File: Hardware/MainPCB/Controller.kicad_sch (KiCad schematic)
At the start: 31 parts, among them J10 Conn_01x02_Male, J11 Conn_01x11_Male, SW1 SW_Push, SW2 SW_Push, SW3 SW_Push, SW4 SW_Push, U5 CP2102N-Axx-xQFN28, U6 ATmega4809-A, U7 LMH1980

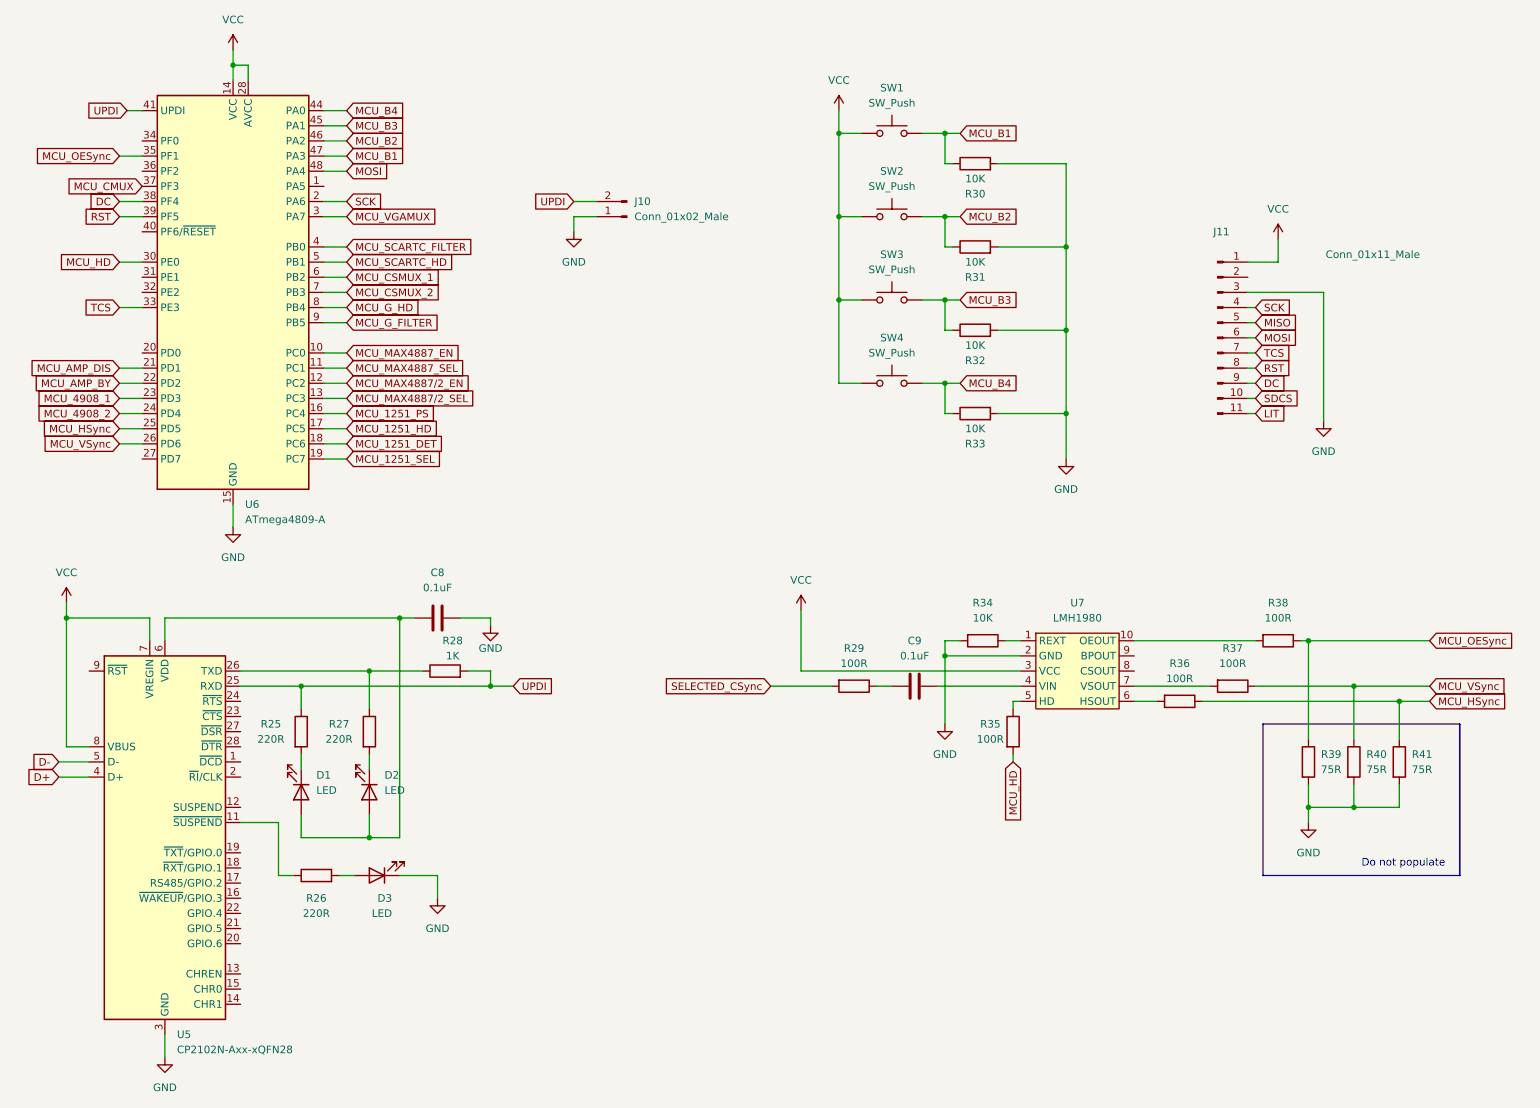
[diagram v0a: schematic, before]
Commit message: Fixed color bending issue; Added diagnostics
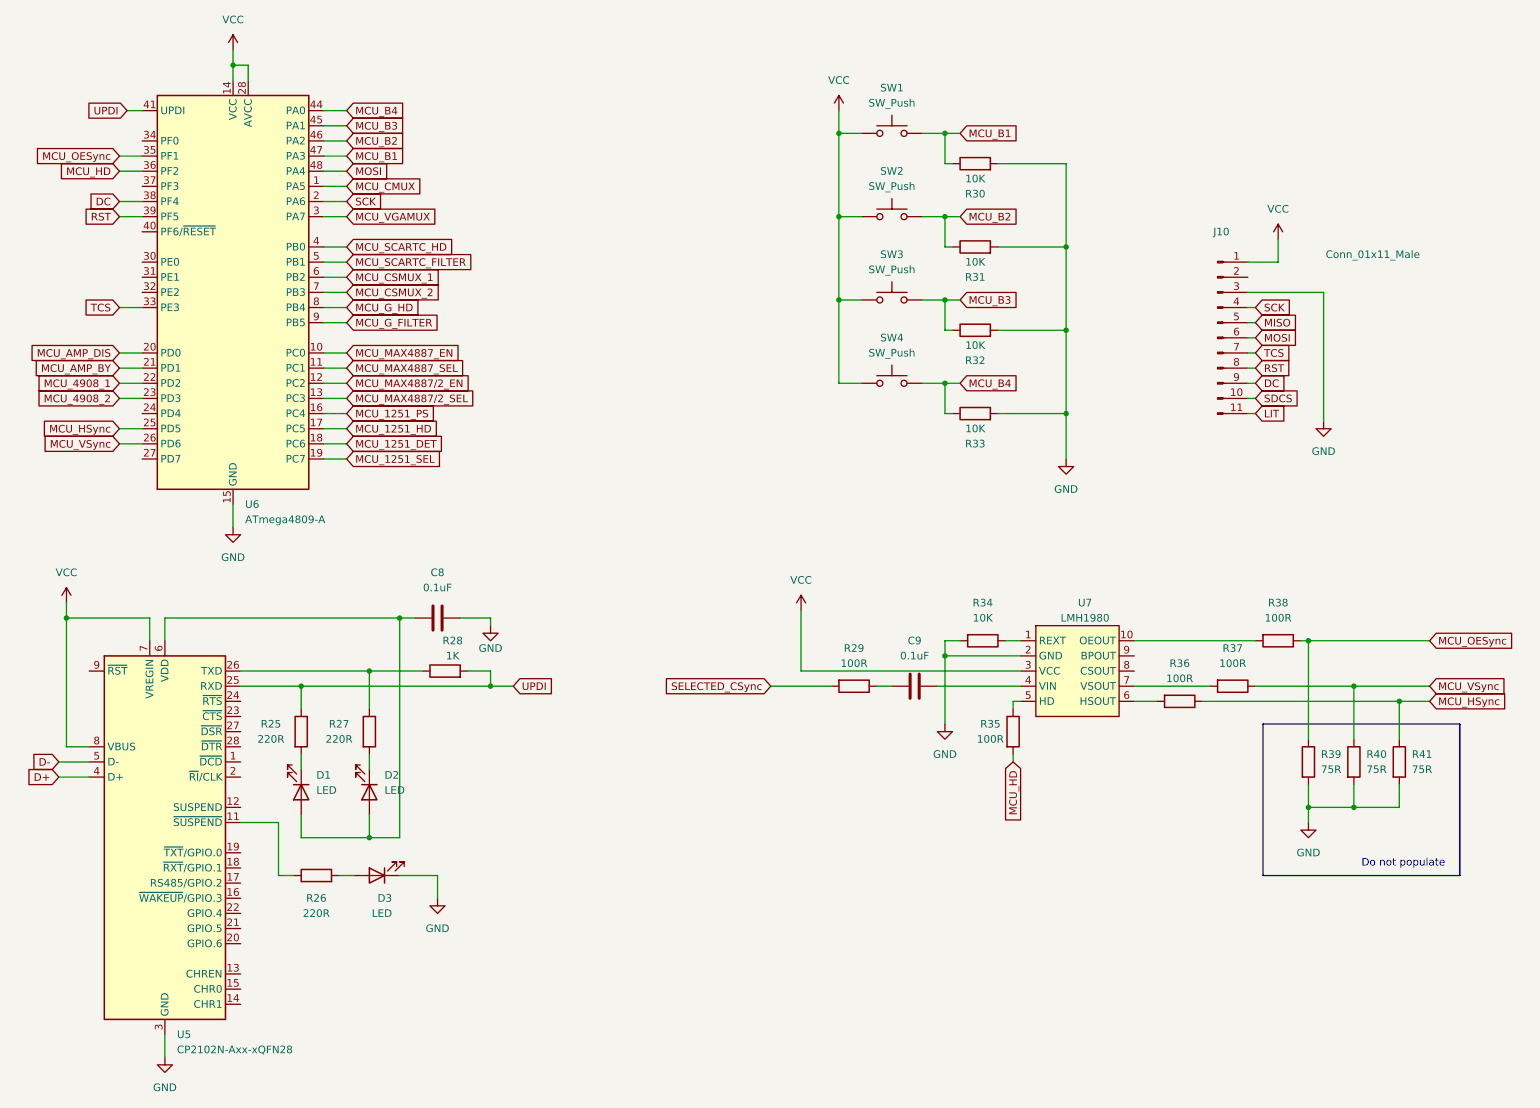
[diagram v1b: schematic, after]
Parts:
- removed J10: Conn_01x02_Male, Connector_PinSocket_2.54mm:PinSocket_1x02_P2.54mm_Vertical, symbol Connector:Conn_01x02_Male
- R25, R26, R27, R28, R29, R30, R31, R32, R33, R34, R35, R36, R37, R38, R39, R40, R41: footprint Resistor_SMD:R_0603_1608Metric -> RT5XP-EXP:R_0603; symbol Device:R -> RT5XP_EXP:R
- U7: footprint Package_SO:VSSOP-10_3x3mm_P0.5mm -> RT5XP-EXP:VSSOP-10_3x3mm_P0.5mm; symbol AE:LMH1980 -> RT5XP_EXP:LMH1980
- renumbered J11 to J10
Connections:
- net MCU_4908_1: now also U6.22 (PD2); no longer U6.23 (PD3)
- net MCU_4908_2: now also U6.23 (PD3); no longer U6.24 (PD4)
- net MCU_AMP_BY: now also U6.21 (PD1); no longer U6.22 (PD2)
- net MCU_AMP_DIS: now also U6.20 (PD0); no longer U6.21 (PD1)
- net MCU_CMUX: now also U6.1 (PA5); no longer U6.37 (PF3)
- net MCU_HD: now also U6.36 (PF2); no longer U6.30 (PE0)
- net MCU_SCARTC_FILTER: now also U6.5 (PB1); no longer U6.4 (PB0)
- net MCU_SCARTC_HD: now also U6.4 (PB0); no longer U6.5 (PB1)
